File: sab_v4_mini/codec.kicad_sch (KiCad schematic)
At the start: 9 parts

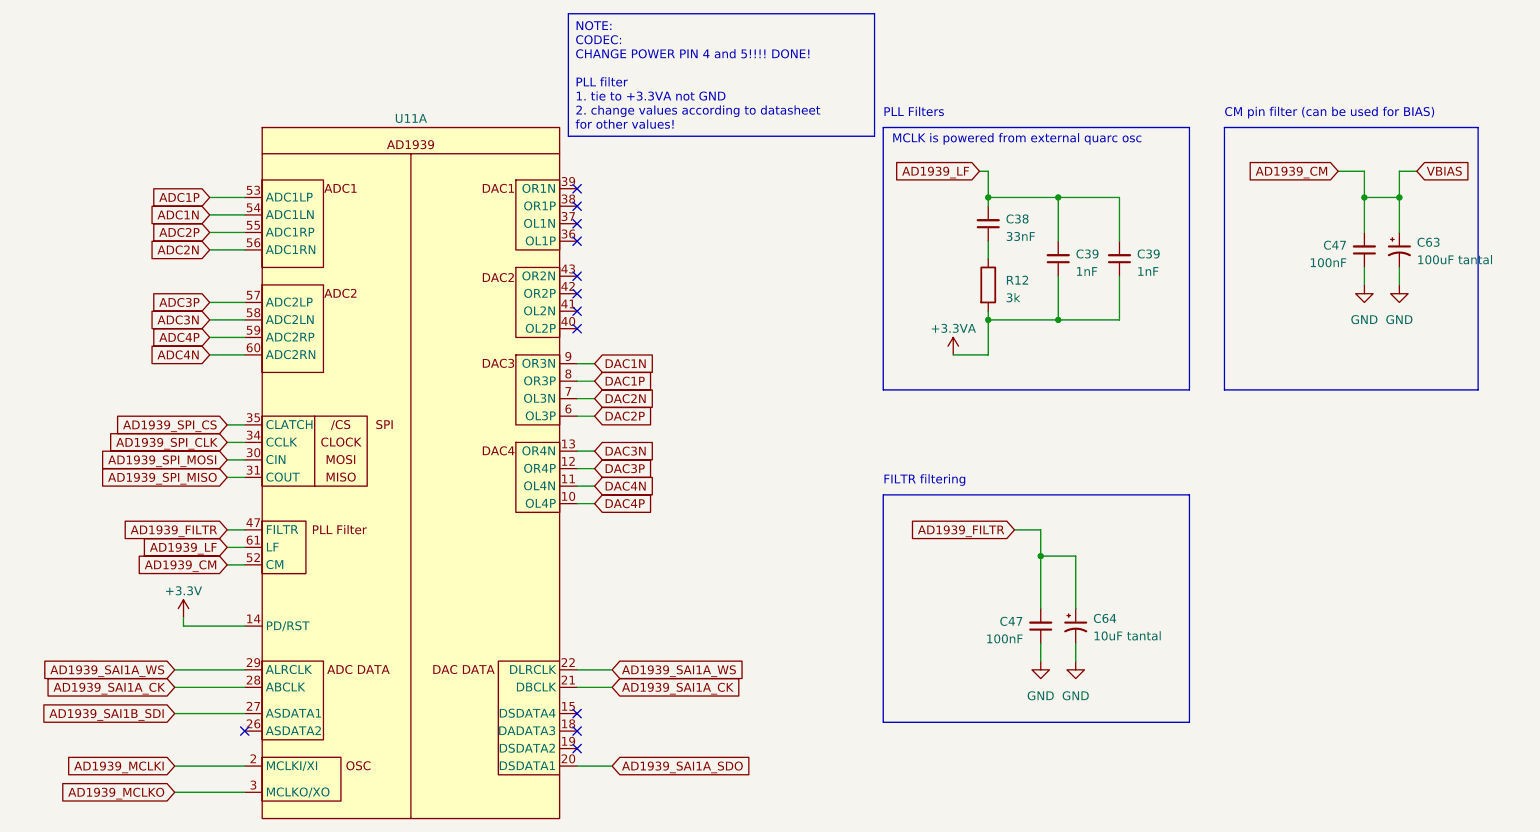
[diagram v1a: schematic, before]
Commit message: added codec
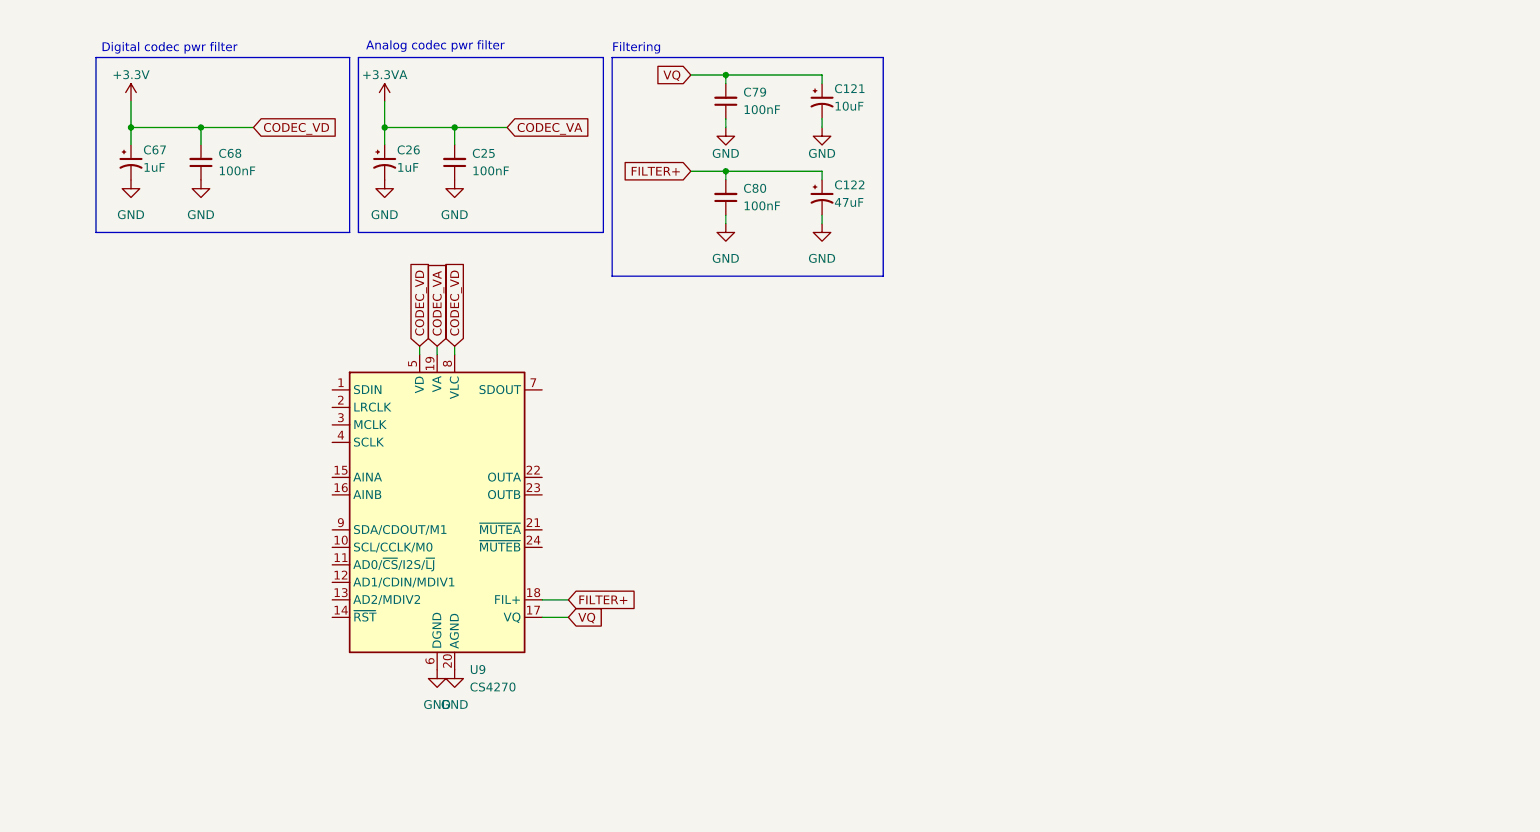
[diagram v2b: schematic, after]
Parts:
- removed C38: 33nF, Capacitor_SMD:C_0805_2012Metric_Pad1.18x1.45mm_HandSolder, symbol Device:C_Small
- removed C39 (x2): 1nF, Capacitor_SMD:C_0603_1608Metric, symbol Device:C_Small
- removed C47 (x2): 100nF, Capacitor_SMD:C_0603_1608Metric, symbol Device:C_Small
- removed C63: 100uF tantal, Capacitor_Tantalum_SMD:CP_EIA-3528-21_Kemet-B, symbol Device:C_Polarized_Small_US
- removed C64: 10uF tantal, Capacitor_Tantalum_SMD:CP_EIA-3216-18_Kemet-A, symbol Device:C_Polarized_Small_US
- removed R12: 3k, Resistor_SMD:R_0603_1608Metric, symbol Device:R
- removed U11: ~, Package_QFP:LQFP-64_10x10mm_P0.5mm, symbol codec:AD1939
- added C121: 10uF, stm_audio_board_footprints:CP_Radial_D6.3mm_P2.50mm_reference_fix, symbol Device:C_Polarized_Small_US
- added C122: 47uF, stm_audio_board_footprints:CP_Radial_D6.3mm_P2.50mm_reference_fix, symbol Device:C_Polarized_Small_US
- added C25, C68, C79, C80: 100nF, Capacitor_SMD:C_0603_1608Metric, symbol Device:C_Small
- added C26, C67: 1uF, stm_audio_board_footprints:CP_Radial_D6.3mm_P2.50mm_reference_fix, symbol Device:C_Polarized_Small_US
- added U9: CS4270, Package_SO:TSSOP-24_4.4x7.8mm_P0.65mm, symbol Audio:CS4270
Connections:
- net +3.3V: now also C67.1, C68.2, U9.5 (VD), U9.8 (VLC)
- net +3.3VA: now also C25.2, C26.1, U9.19 (VA)
- net GND: now also C121.2, C122.2, C25.1, C26.2, C67.2, C68.1, C79.1, C80.1, U9.20 (AGND), U9.6 (DGND)
- new net FILTER+: C122.1, C80.2, U9.18 (FIL+)
- new net VQ: C121.1, C79.2, U9.17 (VQ)
- no-connect marks 12 -> 0
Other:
- note added: "Analog codec pwr filter"
- note added: "Digital codec pwr filter"
- note added: "Filtering"
- note removed: "CM pin filter (can be used for BIAS)"
- note removed: "FILTR filtering"
- note removed: "MCLK is powered from external quarc osc"
- note removed: "PLL Filters"

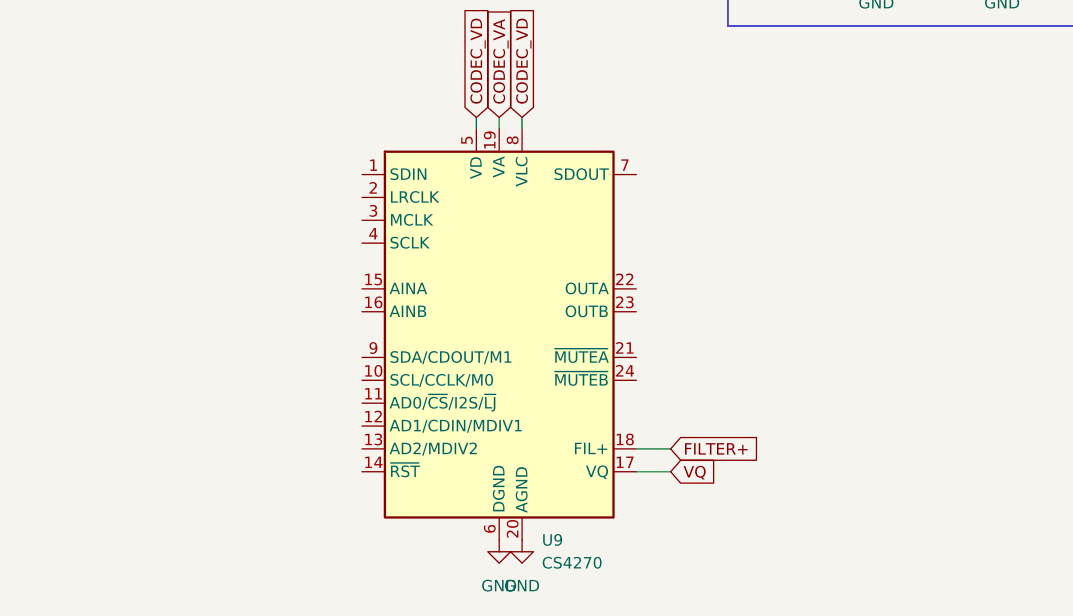
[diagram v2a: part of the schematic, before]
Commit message: moved codec
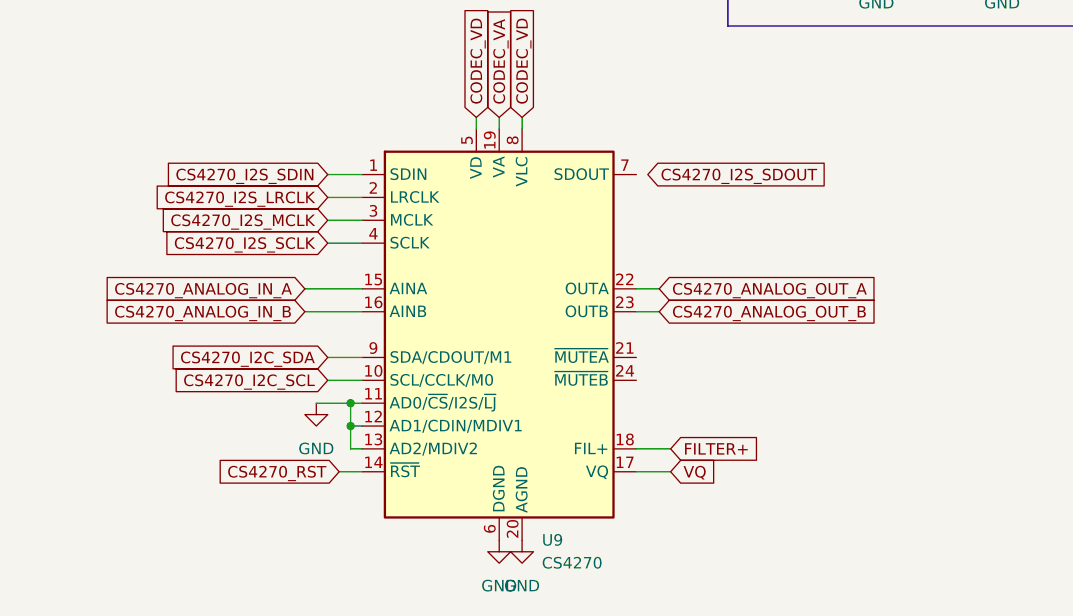
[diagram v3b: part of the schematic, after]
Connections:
- net GND: now also U9.11 (AD0/~{CS}/I2S/~{LJ}), U9.12 (AD1/CDIN/MDIV1), U9.13 (AD2/MDIV2)
- net CS4270_I2S_SDIN: now reaches U9.1 (SDIN)
- net CS4270_I2C_SCL: now reaches U9.10 (SCL/CCLK/M0)
- net CS4270_RST: now reaches U9.14 (~{RST})
- net CS4270_ANALOG_IN_A: now reaches U9.15 (AINA)
- net CS4270_ANALOG_IN_B: now reaches U9.16 (AINB)
- net CS4270_I2S_LRCLK: now reaches U9.2 (LRCLK)
- net CS4270_ANALOG_OUT_A: now reaches U9.22 (OUTA)
- net CS4270_ANALOG_OUT_B: now reaches U9.23 (OUTB)
- net CS4270_I2S_MCLK: now reaches U9.3 (MCLK)
- net CS4270_I2S_SCLK: now reaches U9.4 (SCLK)
- net CS4270_I2C_SDA: now reaches U9.9 (SDA/CDOUT/M1)
